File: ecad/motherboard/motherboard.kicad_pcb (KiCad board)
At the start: 2 copper layers, 199.5 x 99.5 mm, 207 parts, among them J1 B6B-XH-A(LF)(SN), J2 Amphenol_10061913-xx0, J3 Amphenol_10061913-xx0, J4 Amphenol_10061913-xx0, J5 Amphenol_10061913-xx0, J6 Amphenol_10061913-xx0, J7 Amphenol_10061913-xx0, J8 Amphenol_10061913-xx0, J9 Amphenol_10061913-xx0, U1 CD4051BPWR4, U10 TLP4026G, U11 TLP4026G, U12 NE5532, U13 TLP4026G, U14 TLP4026G, U15 NE5532, U16 TLP4026G, U17 TLP4026G, U18 TCA9544APWR, U19 CD4051BPWR4, U2 NodeMCU ESP-32S, U20 CD4051BPWR4, U21 NE5532, U22 TLP4026G, U23 TLP4026G, U24 NE5532, U25 TLP4026G, U26 TLP4026G, U27 NE5532, U28 TLP4026G, U29 TLP4026G, U3 TCA9544APWR, U30 NE5532, U31 TLP4026G, U32 TLP4026G, U33 NE5532, U34 PGA231x, U4 CD4051BPWR4, U5 CD4051BPWR4, U6 NE5532, U7 TLP4026G, U8 TLP4026G, U9 NE5532

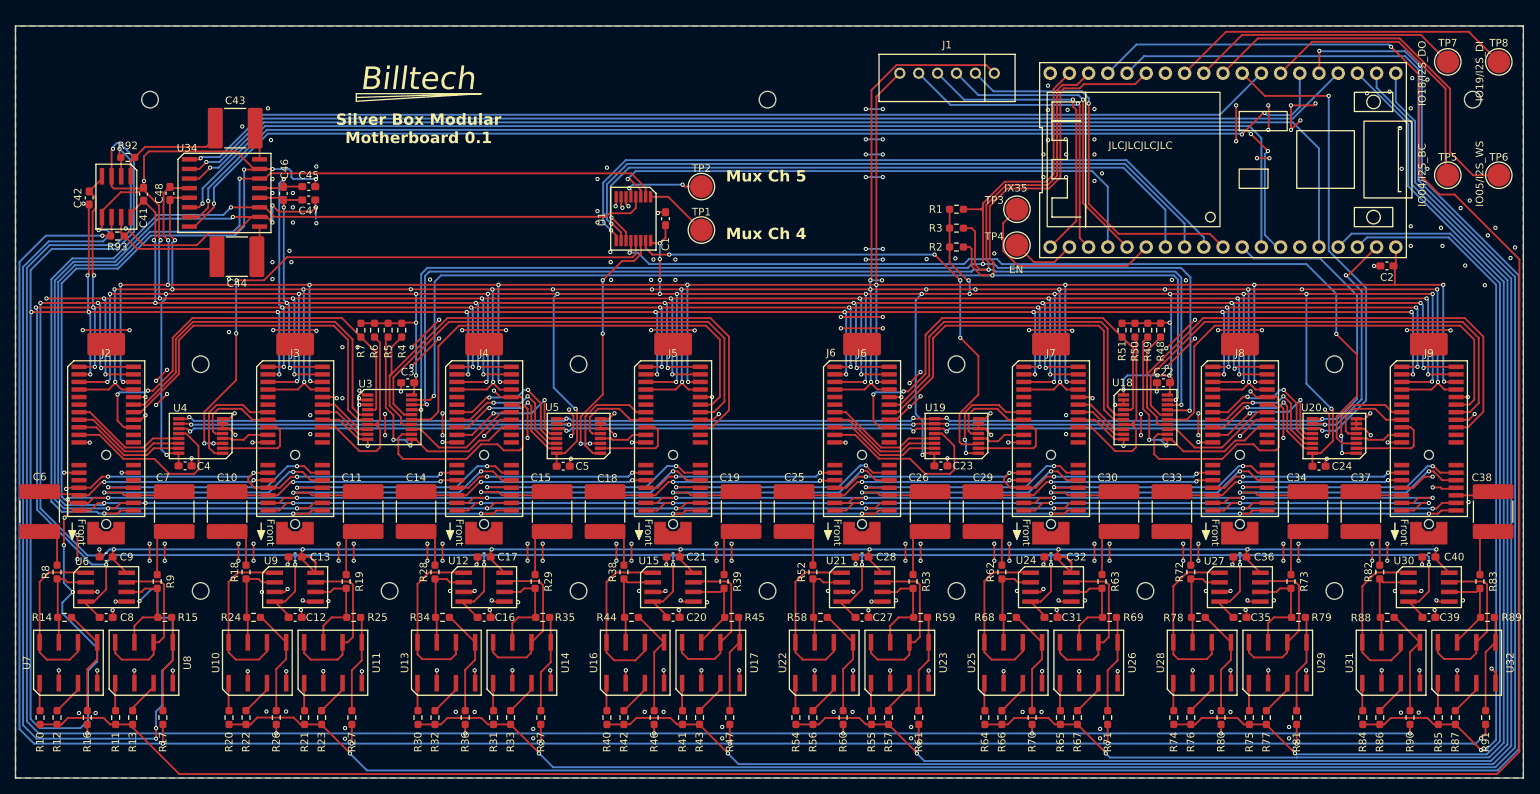
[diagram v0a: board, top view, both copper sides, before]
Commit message: Updates and additions for peripheral test board and power supply prototype
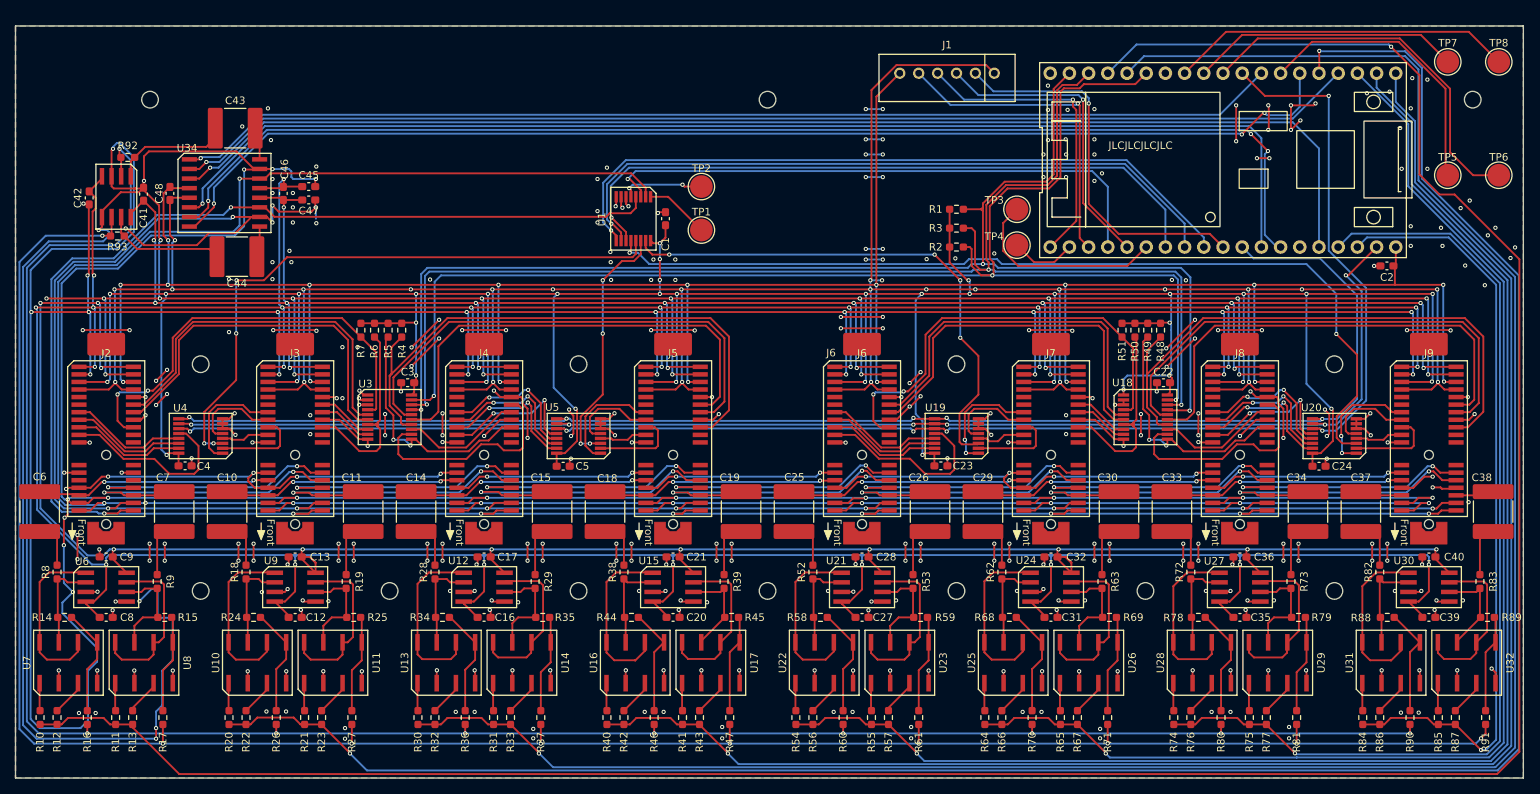
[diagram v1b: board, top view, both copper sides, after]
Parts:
- removed the REF** at (112.0, 58.0)
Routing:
- net +3V3: vias 38 -> 37
- net GND: vias 483 -> 482
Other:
- board text removed: "EN"
- board text removed: "IO04/I2S_BC"
- board text removed: "IO05/I2S_WS"
- board text removed: "IO18/I2S_DO"
- board text removed: "IO19/I2S_DI"
- board text removed: "IX35"
- board text removed: "Mux Ch 4"
- board text removed: "Mux Ch 5"
- board text removed: "Silver Box Modular Motherboard 0.1"

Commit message: Add manufacturer part numbers into Kicad Schematics
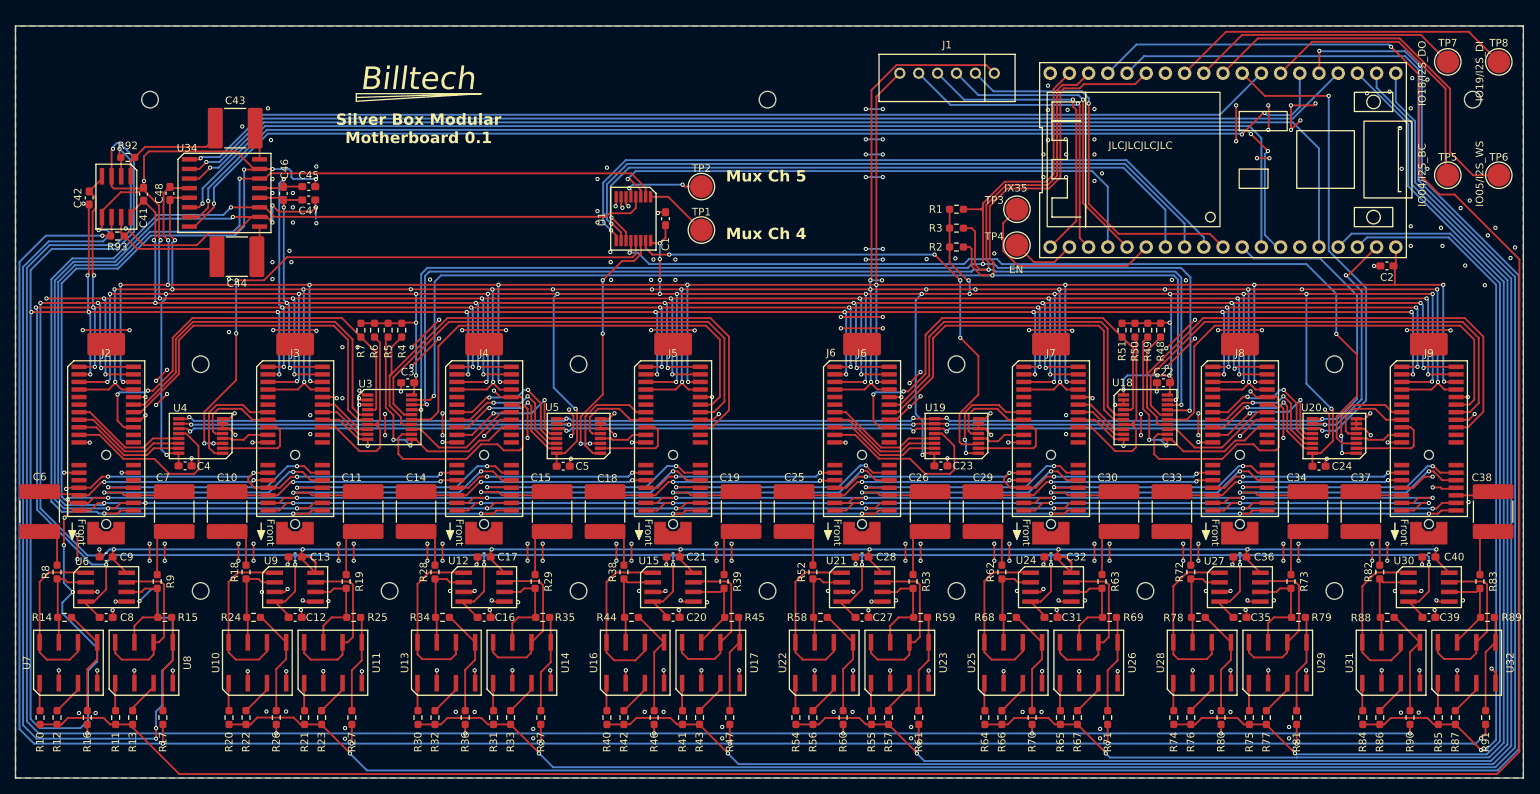
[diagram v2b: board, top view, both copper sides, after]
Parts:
- added REF**: Billtech, silver-box-feetprints:Billtech, F.Cu at (112.0, 58.0)
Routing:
- net +3V3: vias 37 -> 38
- net GND: vias 482 -> 483
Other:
- board text added: "EN"
- board text added: "IO04/I2S_BC"
- board text added: "IO05/I2S_WS"
- board text added: "IO18/I2S_DO"
- board text added: "IO19/I2S_DI"
- board text added: "IX35"
- board text added: "Mux Ch 4"
- board text added: "Mux Ch 5"
- board text added: "Silver Box Modular Motherboard 0.1"
